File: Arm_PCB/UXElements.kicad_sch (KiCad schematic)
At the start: 31 parts

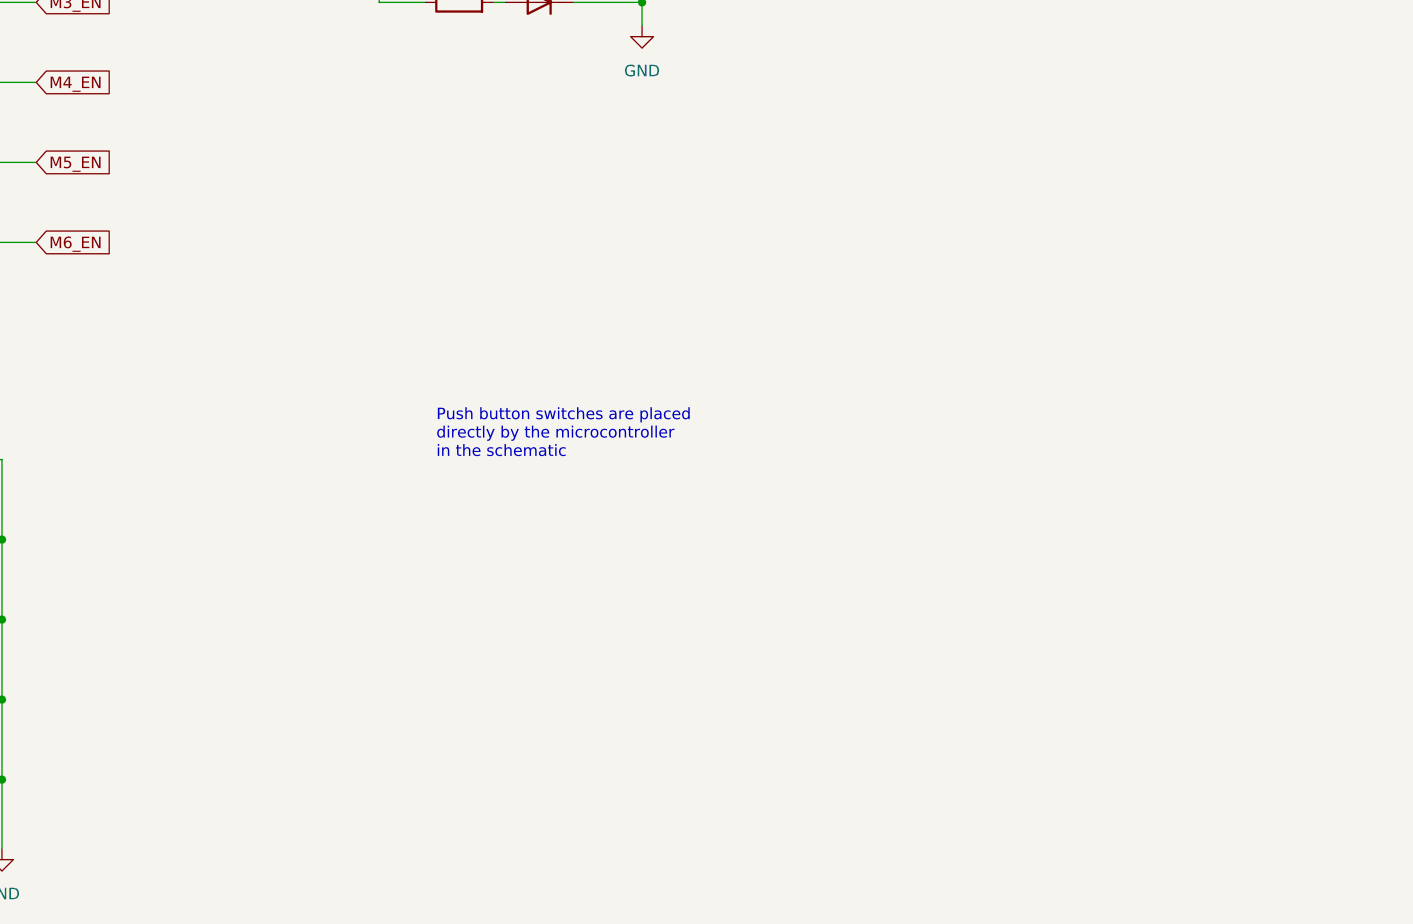
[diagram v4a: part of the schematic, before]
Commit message: Add spotlight and resistors on limit switches
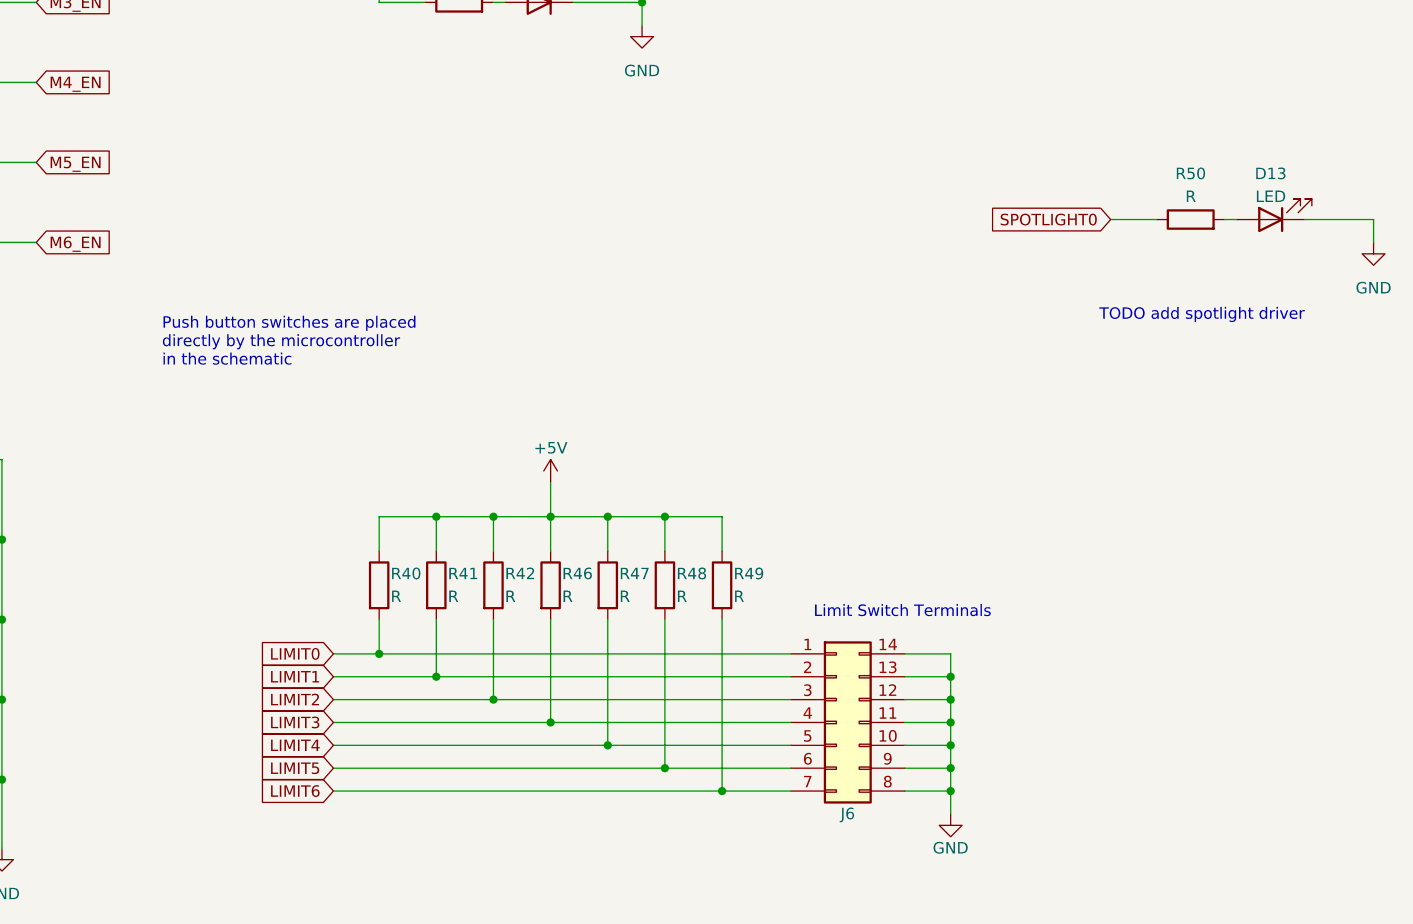
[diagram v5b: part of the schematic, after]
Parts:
- added D13: LED, symbol Device:LED
- added J6: Conn_02x07_Counter_Clockwise, symbol Connector_Generic:Conn_02x07_Counter_Clockwise
- added R40, R41, R42, R46, R47, R48, R49, R50: R, symbol Device:R
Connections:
- net +5V: now also R40.1, R41.1, R42.1, R46.1, R47.1, R48.1, R49.1
- net GND: now also D13.1 (K), J6.10 (Pin_10), J6.11 (Pin_11), J6.12 (Pin_12), J6.13 (Pin_13), J6.14 (Pin_14), J6.8 (Pin_8), J6.9 (Pin_9)
- new net: D13.2 (A), R50.2
- new net LIMIT0: J6.1 (Pin_1), R40.2
- new net LIMIT1: J6.2 (Pin_2), R41.2
- new net LIMIT2: J6.3 (Pin_3), R42.2
- new net LIMIT3: J6.4 (Pin_4), R46.2
- new net LIMIT4: J6.5 (Pin_5), R47.2
- new net LIMIT5: J6.6 (Pin_6), R48.2
- new net LIMIT6: J6.7 (Pin_7), R49.2
- new net SPOTLIGHT0: R50.1
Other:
- note added: "Limit Switch Terminals"
- note added: "TODO add spotlight driver"

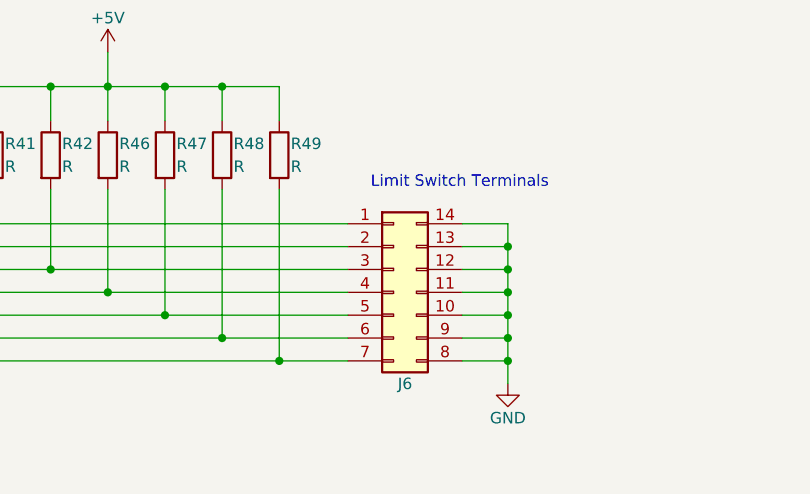
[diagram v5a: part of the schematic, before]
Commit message: Added a basic footprint for the PCB
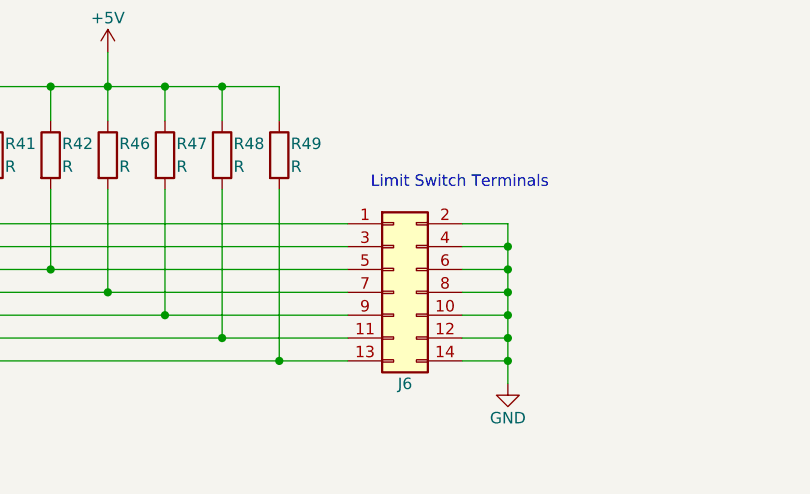
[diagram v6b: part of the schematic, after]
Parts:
- BZ1: footprint (none) -> Buzzer_Beeper:Buzzer_12x9.5RM7.6
- D1, D10, D11, D12, D13, D16, D17, D18, D2, D3, D4, D5, D6, D7, D8, D9: footprint (none) -> LED_SMD:LED_1206_3216Metric_Pad1.42x1.75mm_HandSolder
- J6: footprint (none) -> Connector_PinHeader_2.54mm:PinHeader_2x07_P2.54mm_Vertical; symbol Connector_Generic:Conn_02x07_Counter_Clockwise -> Connector_Generic:Conn_02x07_Odd_Even
- R28, R29, R30, R31, R32, R33, R34, R35, R36, R37, R38, R39, R40, R41, R42, R43, R44, R45, R46, R47, R48, R49, R50: footprint (none) -> Resistor_SMD:R_1206_3216Metric_Pad1.30x1.75mm_HandSolder
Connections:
- net GND: now also J6.2 (Pin_2), J6.4 (Pin_4), J6.6 (Pin_6); no longer J6.11 (Pin_11), J6.13 (Pin_13), J6.9 (Pin_9)
- net LIMIT1: now also J6.3 (Pin_3); no longer J6.2 (Pin_2)
- net LIMIT2: now also J6.5 (Pin_5); no longer J6.3 (Pin_3)
- net LIMIT3: now also J6.7 (Pin_7); no longer J6.4 (Pin_4)
- net LIMIT4: now also J6.9 (Pin_9); no longer J6.5 (Pin_5)
- net LIMIT5: now also J6.11 (Pin_11); no longer J6.6 (Pin_6)
- net LIMIT6: now also J6.13 (Pin_13); no longer J6.7 (Pin_7)

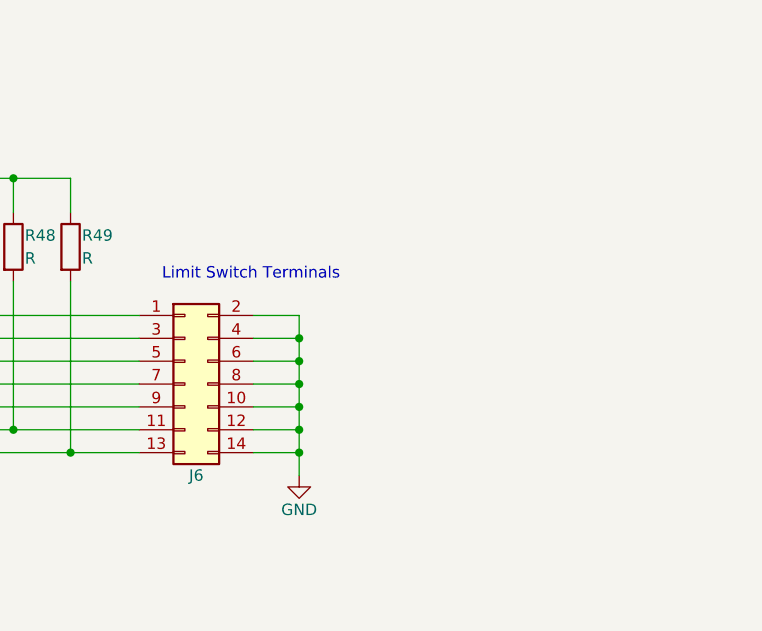
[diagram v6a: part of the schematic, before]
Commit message: Create good footprint for TB6560 driver
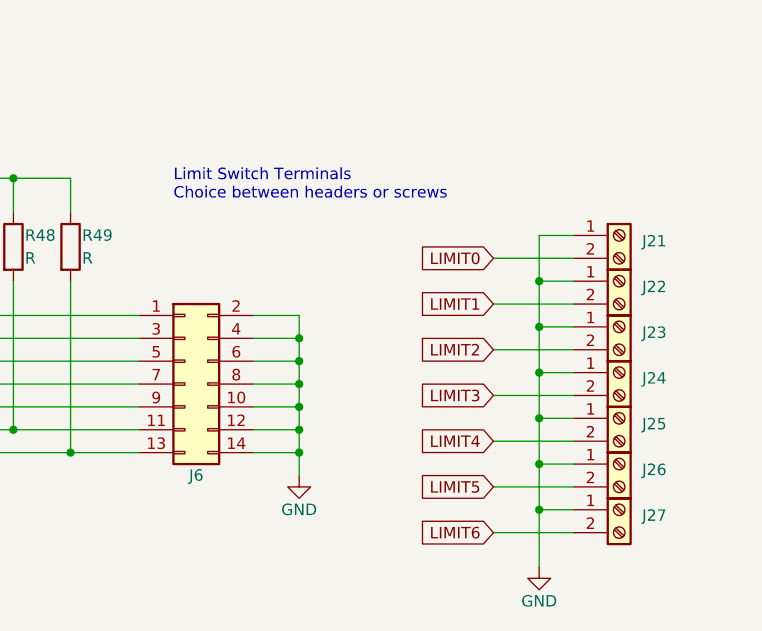
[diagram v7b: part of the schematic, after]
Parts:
- added J21, J22, J23, J24, J25, J26, J27: Screw_Terminal_01x02, TerminalBlock:TerminalBlock_bornier-2_P5.08mm, symbol Connector:Screw_Terminal_01x02
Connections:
- net GND: now also J21.1 (Pin_1), J22.1 (Pin_1), J23.1 (Pin_1), J24.1 (Pin_1), J25.1 (Pin_1), J26.1 (Pin_1), J27.1 (Pin_1)
- net LIMIT0: now also J21.2 (Pin_2)
- net LIMIT1: now also J22.2 (Pin_2)
- net LIMIT2: now also J23.2 (Pin_2)
- net LIMIT3: now also J24.2 (Pin_2)
- net LIMIT4: now also J25.2 (Pin_2)
- net LIMIT5: now also J26.2 (Pin_2)
- net LIMIT6: now also J27.2 (Pin_2)
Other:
- note added: "Limit Switch Terminals Choice between headers or screws"
- note removed: "Limit Switch Terminals"

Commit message: Continue layout, pick some components
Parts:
- BZ1: footprint Buzzer_Beeper:Buzzer_12x9.5RM7.6 -> Buzzer_Beeper:Buzzer_15x7.5RM7.6
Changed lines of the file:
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@@
       (effects (font (size 1.27 1.27)) (justify left))
     )
-    (property "Footprint" "Buzzer_Beeper:Buzzer_12x9.5RM7.6" (at 178.435 39.37 90)
+    (property "Footprint" "Buzzer_Beeper:Buzzer_15x7.5RM7.6" (at 178.435 39.37 90)
       (effects (font (size 1.27 1.27)) hide)
     )
